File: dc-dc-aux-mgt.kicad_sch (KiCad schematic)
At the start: 42 parts, among them U19 MPM54304GMN, U25 PAC1720-1, U3 PAC1720-1

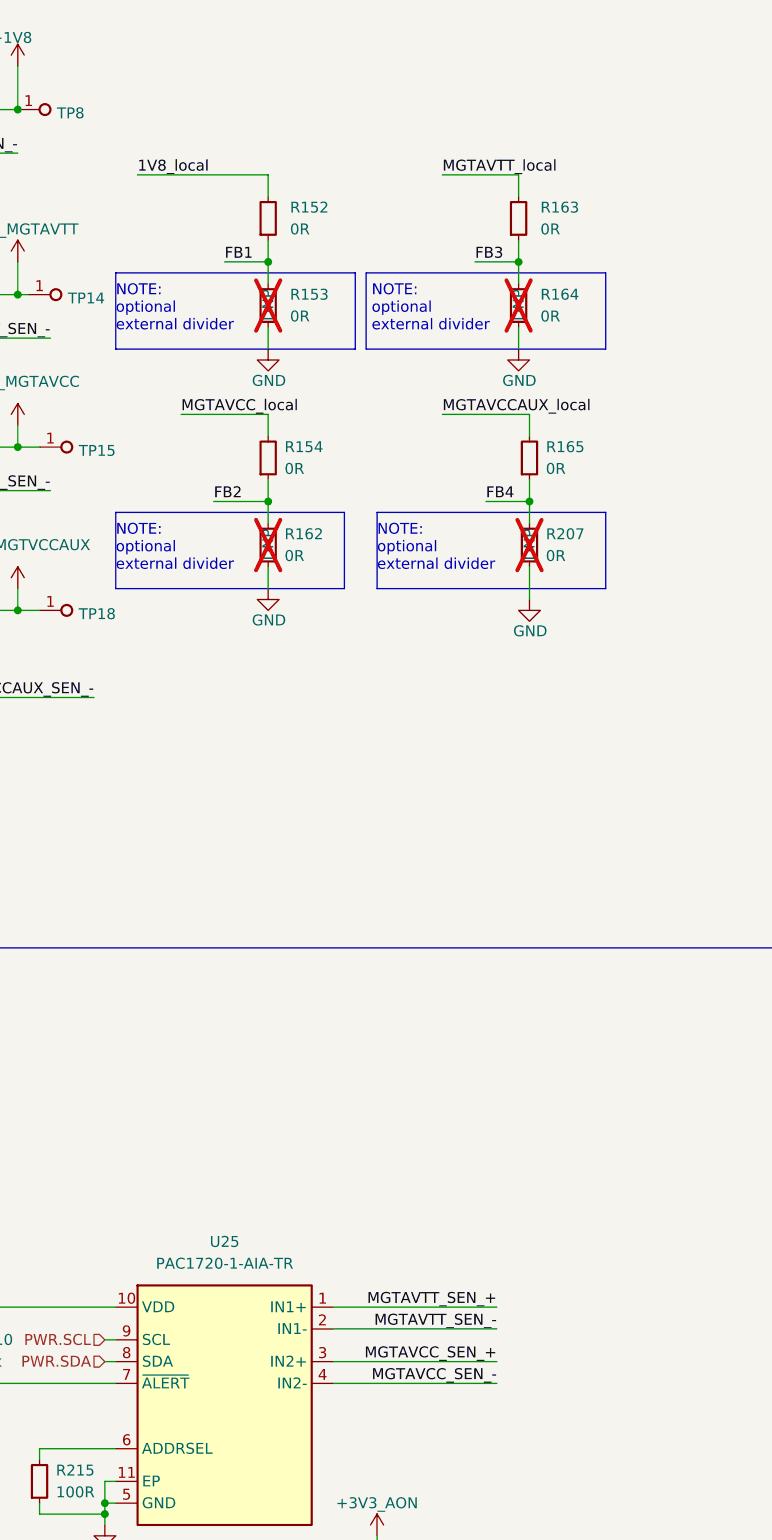
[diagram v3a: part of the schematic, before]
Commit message: [#67725] Import review changes to PCB. Minor schematic fix
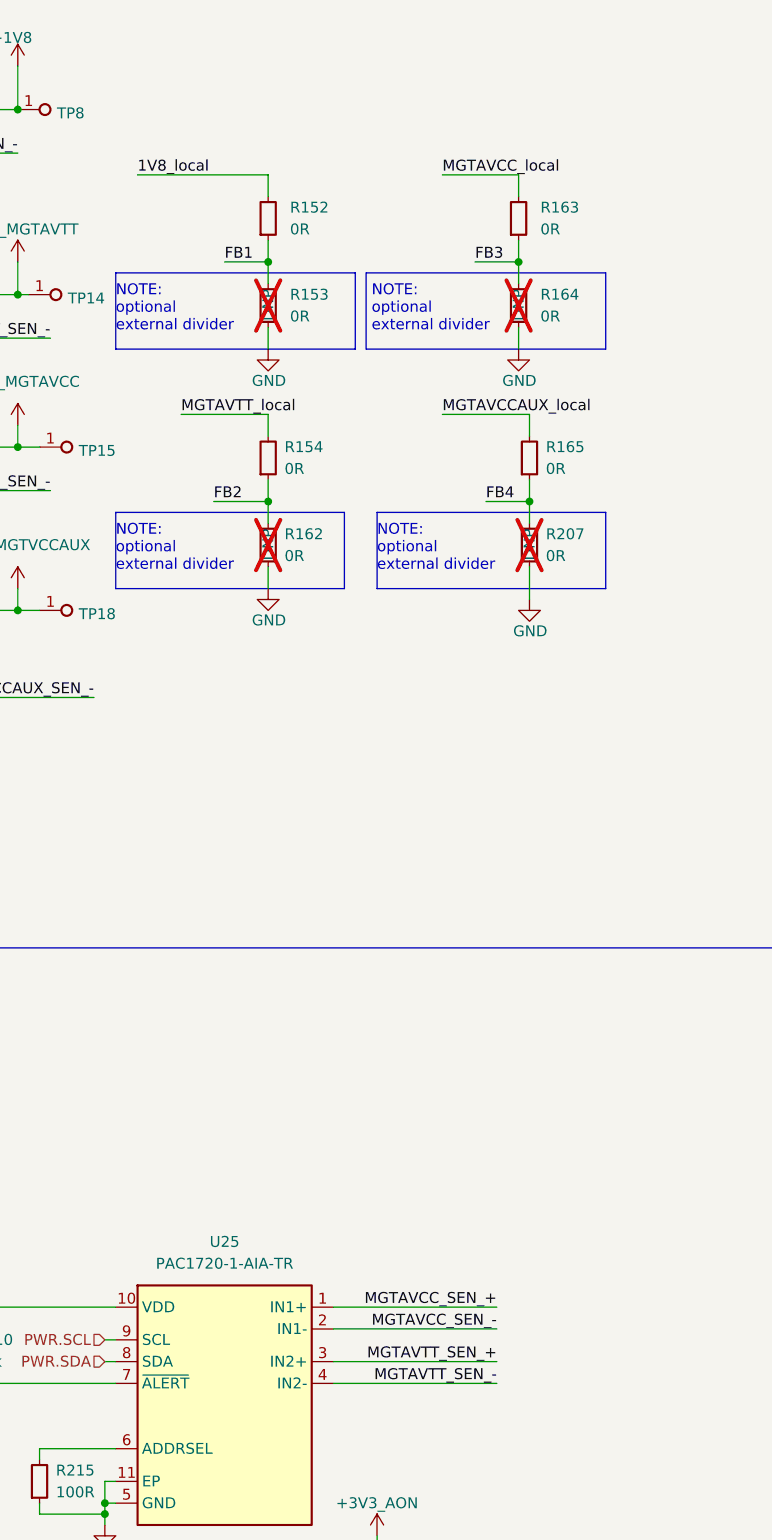
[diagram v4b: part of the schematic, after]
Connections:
- net MGTAVCC_SEN_+: now also U25.1 (IN1+); no longer U25.3 (IN2+)
- net MGTAVCC_SEN_-: now also U25.2 (IN1-); no longer U25.4 (IN2-)
- net MGTAVCC_local: now also R163.2; no longer R154.2
- net MGTAVTT_SEN_+: now also U25.3 (IN2+); no longer U25.1 (IN1+)
- net MGTAVTT_SEN_-: now also U25.4 (IN2-); no longer U25.2 (IN1-)
- net MGTAVTT_local: now also R154.2; no longer R163.2
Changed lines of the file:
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@@
     (effects (font (size 1.27 1.27)) (justify left bottom))
   )
-  (label "MGTAVCC_local" (at 248.92 88.9 0) (fields_autoplaced)
+  (label "MGTAVCC_local" (at 279.4 60.96 0) (fields_autoplaced)
     (effects (font (size 1.27 1.27)) (justify left bottom))
   )
-  (label "MGTAVTT_local" (at 279.4 60.96 0) (fields_autoplaced)
+  (label "MGTAVTT_local" (at 248.92 88.9 0) (fields_autoplaced)
     (effects (font (size 1.27 1.27)) (justify left bottom))
   )
@@
     (effects (font (size 1.27 1.27)) (justify left bottom))
   )
-  (label "MGTAVTT_SEN_-" (at 285.75 195.58 180) (fields_autoplaced)
+  (label "MGTAVTT_SEN_-" (at 285.75 201.93 180) (fields_autoplaced)
     (effects (font (size 1.27 1.27)) (justify right bottom))
   )
-  (label "MGTAVTT_SEN_+" (at 285.75 193.04 180) (fields_autoplaced)
+  (label "MGTAVTT_SEN_+" (at 285.75 199.39 180) (fields_autoplaced)
     (effects (font (size 1.27 1.27)) (justify right bottom))
   )
@@
     (effects (font (size 1.27 1.27)) (justify left bottom))
   )
-  (label "MGTAVCC_SEN_-" (at 285.75 201.93 180) (fields_autoplaced)
+  (label "MGTAVCC_SEN_-" (at 285.75 195.58 180) (fields_autoplaced)
     (effects (font (size 1.27 1.27)) (justify right bottom))
   )
@@
     (effects (font (size 1.27 1.27)) (justify left bottom))
   )
-  (label "MGTAVCC_SEN_+" (at 285.75 199.39 180) (fields_autoplaced)
+  (label "MGTAVCC_SEN_+" (at 285.75 193.04 180) (fields_autoplaced)
     (effects (font (size 1.27 1.27)) (justify right bottom))
   )

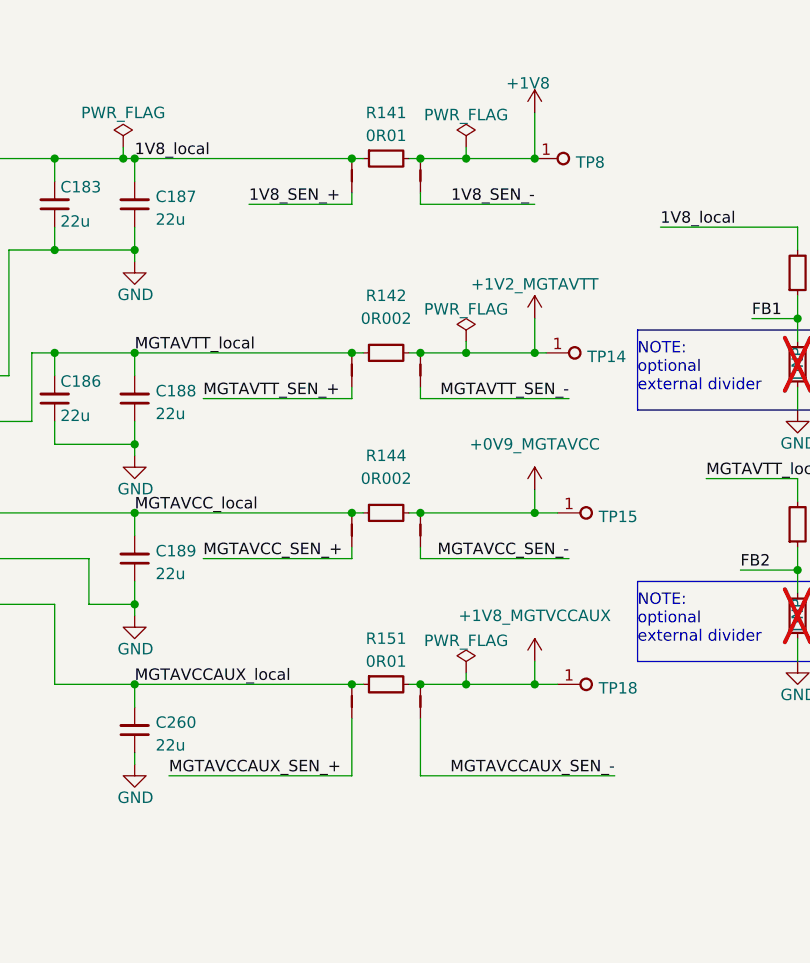
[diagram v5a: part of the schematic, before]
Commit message: [#68016] Solve ERC warrings and errors
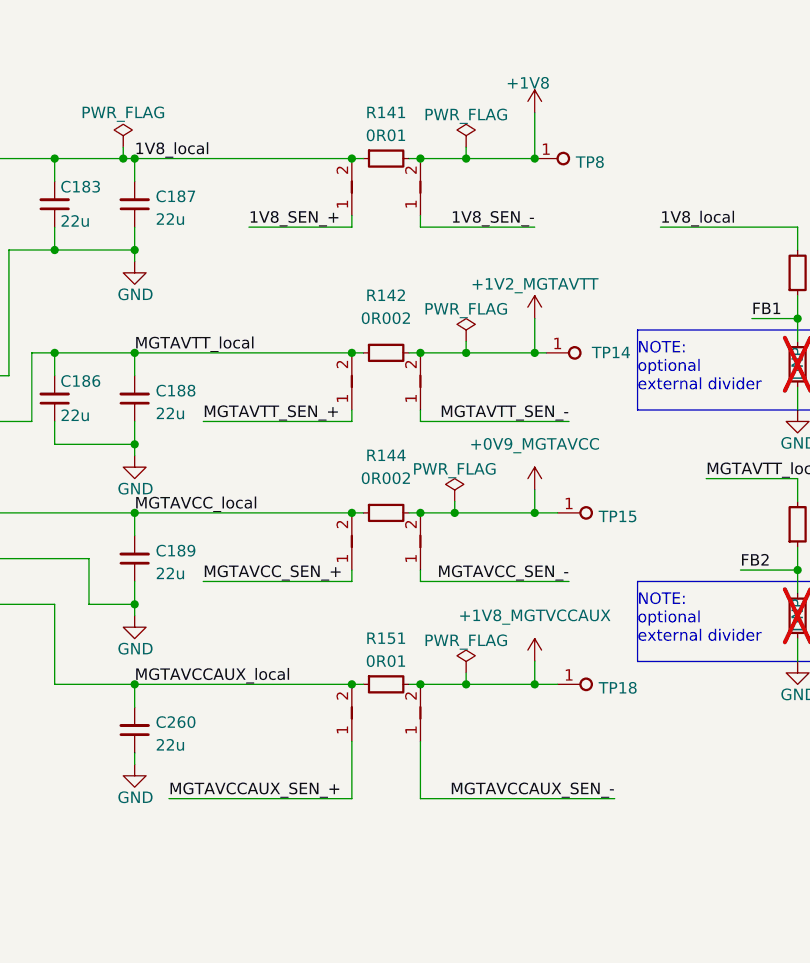
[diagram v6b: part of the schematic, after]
